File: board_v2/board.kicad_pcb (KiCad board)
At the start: 2 copper layers, 136.4 x 81.3 mm, 246 parts, among them J1 DX07S016JA, J10 Conn_01x04_Male, J11 Conn_01x04_Male, J12 Conn_01x04_Male, J13 Conn_01x01_Female, J14 Conn_01x01_Female, J15 Conn_01x01_Female, J16 Conn_01x01_Female, J17 Conn_01x01_Female, J18 Conn_01x09, J3 Conn_01x04_Male, J4 Conn_01x04_Male, J5 Conn_01x04_Male, J6 Conn_01x04_Male, J7 Conn_01x04_Male, J8 Conn_01x04_Male, J9 Conn_01x04_Male, Q1 N-Channel, Q2 N-Channel, Q3 BC857B, Q4 N-Channel, Q5 BC848B, SW1 SW_Push, SW2 SW_Push, SW3 K1-1504SA-03, U1 STM32F103CBTx, U10 TS339, U11 TS339, U12 TS339, U13 USBLC6-4SC6, U14 USBLC6-4SC6, U15 NCP1117-3.3, U16 SGM3204, U17 LM337L, U18 TLV70033, U2 SN74LVC2T45DCT, U3 SN74LVC2T45DCT, U4 USBLC6-4SC6, U5 SN74LVC2T45DCT, U6 SN74LVC2T45DCT, U7 INA240A1, U8 TS339, U9 TS339, X1 SFT_DEBUG_CONNECTOR-SELF, X2 SFT debugport, X3 ARM debugport, X4 Blue, Y1 8.000 MHz

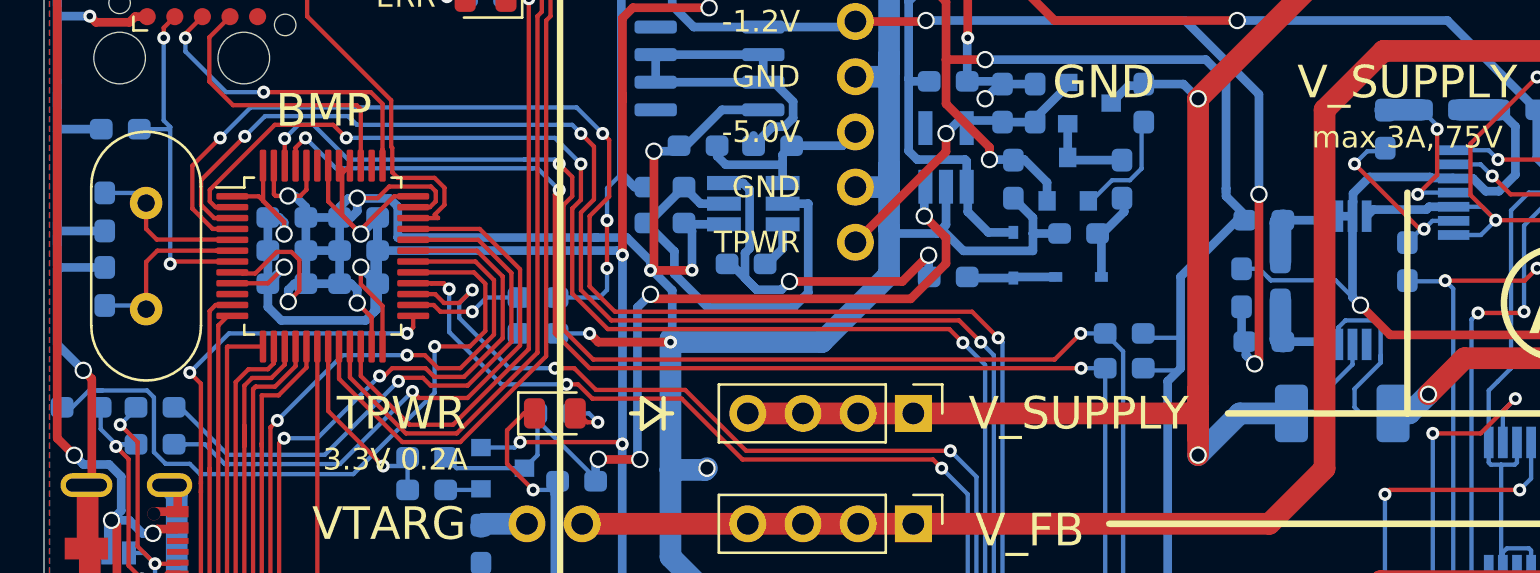
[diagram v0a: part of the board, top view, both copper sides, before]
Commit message: Weird changes to boards after they had been released and ordered
This will not be merged to master but who knows
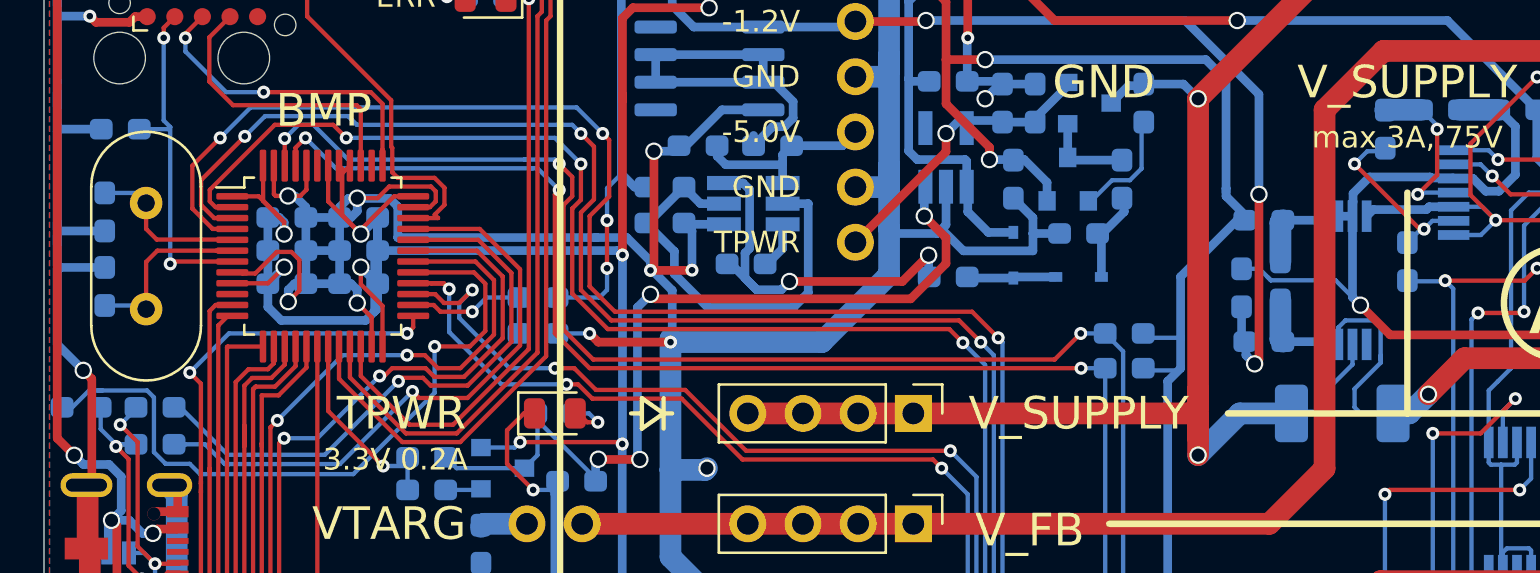
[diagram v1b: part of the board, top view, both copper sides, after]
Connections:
- net /BlackMagicProbe/BMP.~RST renamed /BlackMagicProbe/BMP.~{RST}
- net /BlackMagicProbe/BMP.~TPWR_EN renamed /BlackMagicProbe/BMP.~{TPWR_EN}
- net /BlackMagicProbe/INTERFACE_TARGET_~RST renamed /BlackMagicProbe/INTERFACE_TARGET_~{RST}
- net /BlackMagicProbe/SELF_~RST renamed /BlackMagicProbe/SELF_~{RST}
- net /BlackMagicProbe/UI.~BUTTON_DOWN renamed /BlackMagicProbe/UI.~{BUTTON_DOWN}
- net /BlackMagicProbe/UI.~BUTTON_LEFT renamed /BlackMagicProbe/UI.~{BUTTON_LEFT}
- net /BlackMagicProbe/UI.~BUTTON_PRESS renamed /BlackMagicProbe/UI.~{BUTTON_PRESS}
- net /BlackMagicProbe/UI.~BUTTON_RIGHT renamed /BlackMagicProbe/UI.~{BUTTON_RIGHT}
- net /BlackMagicProbe/UI.~BUTTON_UP renamed /BlackMagicProbe/UI.~{BUTTON_UP}
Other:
- net class Default removed
- net class Massive removed
- net class Power removed
- board text added: "DUT.~{RST}"
- board text added: "DUT.~{RX}"
- board text added: "DUT.~{TX}"
- board text added: "~{RST}"
- board text added: "~{RST} LOW"
- board text added: "~{RXD}"
- board text added: "~{RX} LOW"
- board text added: "~{TXD}"
- board text added: "~{TX} LOW"
- board text removed: "DUT.~RST"
- board text removed: "DUT.~RX"
- board text removed: "DUT.~TX"
- board text removed: "~RST"
- board text removed: "~RST~ LOW"
- board text removed: "~RXD"
- board text removed: "~RX~ LOW"
- board text removed: "~TXD"
- board text removed: "~TX~ LOW"
